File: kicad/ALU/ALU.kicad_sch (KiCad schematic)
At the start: 85 parts, among them J1 Backplane Signal, J2 Backplane Bus, J3 DIN41612_02x32_AC, J4 DIN41612_02x32_AC, U1 74LS377, U10 74LS253, U11 74LS253, U12 74LS253, U13 74LS253, U14 74LS253, U15 74LS253, U16 74LS253, U17 74F382, U18 74F382, U19 74F382, U2 74LS377, U20 74F382, U21 74F382, U22 74LS283, U23 74LS283, U24 74LS283, U25 74LS283, U26 74LS283, U27 74LS244, U28 74LS244, U29 74LS244, U3 74LS377, U30 74LS386, U31 74LS08, U32 74LS32, U33 74LS04, U34 74LS253, U35 74LS27, U36 74LS27, U37 74LS11, U38 74LS257, U39 74LS32, U4 74LS377, U5 74LS377, U6 74LS377, U7 74LS253, U8 74LS253, U9 74LS253

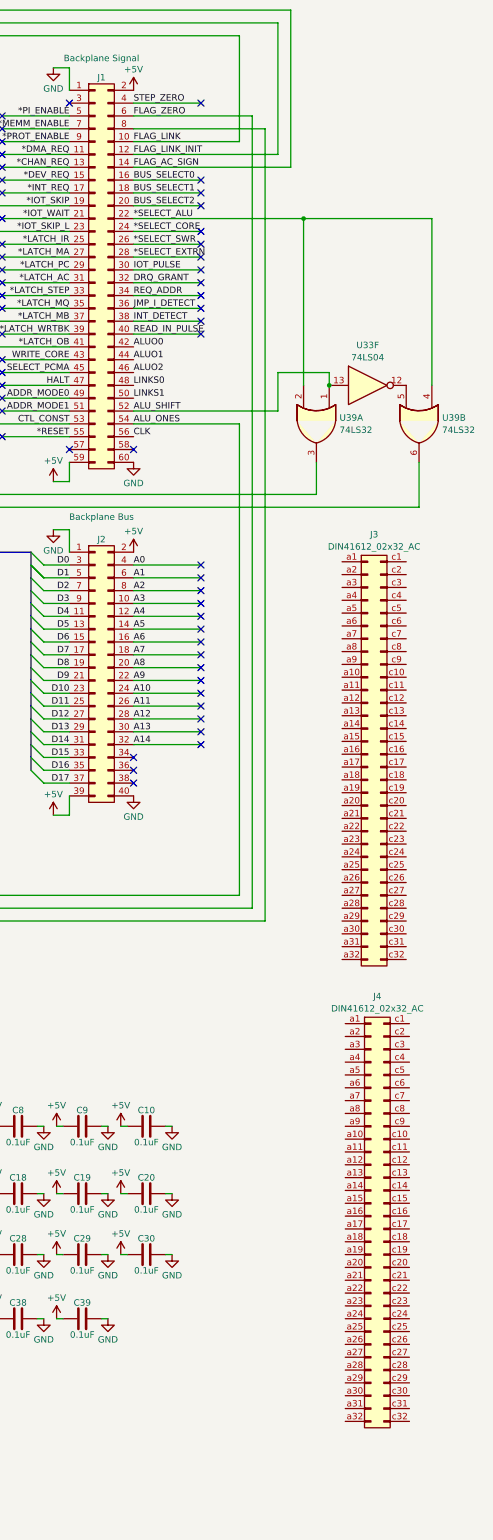
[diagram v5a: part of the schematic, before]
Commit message: Continue connector migration
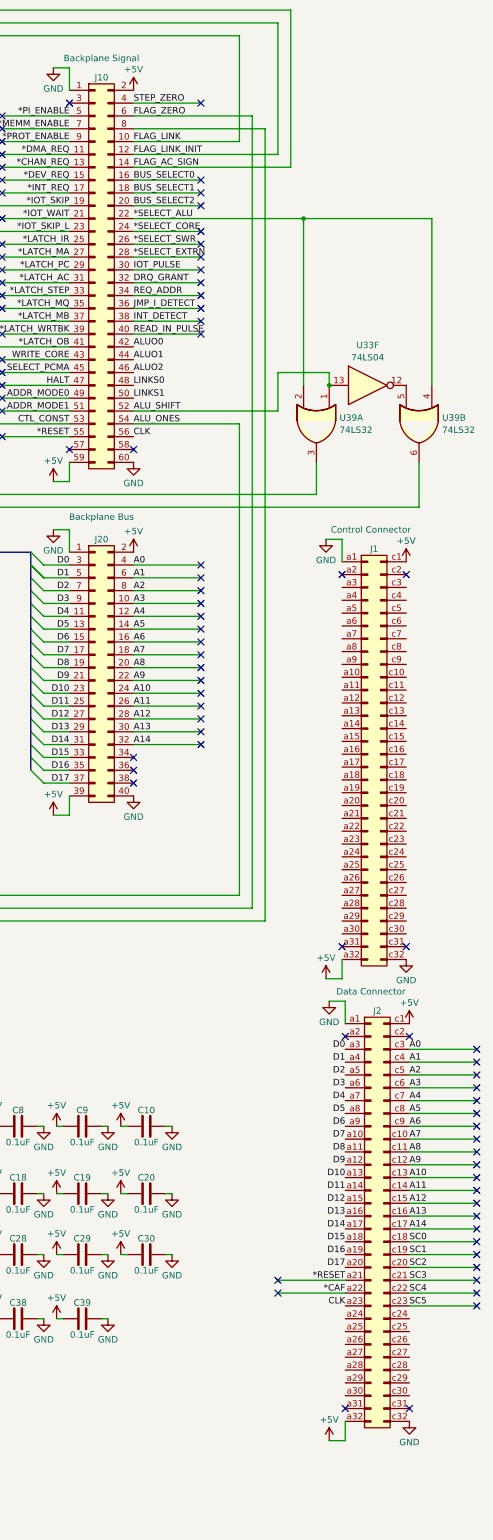
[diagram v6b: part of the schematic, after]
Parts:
- J1: renamed from J3; value DIN41612_02x32_AC -> Control Connector
- J2: renamed from J4; value DIN41612_02x32_AC -> Data Connector
- renumbered J1 to J10, J2 to J20
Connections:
- net *RESET: now also J2.a21 (Pin_a21)
- net +5V: now also J1.a32 (Pin_a32), J1.c1 (Pin_c1), J2.a32 (Pin_a32), J2.c1 (Pin_c1)
- net A0: now also J2.c3 (Pin_c3)
- net A1: now also J2.c4 (Pin_c4)
- net A10: now also J2.c13 (Pin_c13)
- net A11: now also J2.c14 (Pin_c14)
- net A12: now also J2.c15 (Pin_c15)
- net A13: now also J2.c16 (Pin_c16)
- net A14: now also J2.c17 (Pin_c17)
- net A2: now also J2.c5 (Pin_c5)
- net A3: now also J2.c6 (Pin_c6)
- net A4: now also J2.c7 (Pin_c7)
- net A5: now also J2.c8 (Pin_c8)
- net A6: now also J2.c9 (Pin_c9)
- net A7: now also J2.c10 (Pin_c10)
- net A8: now also J2.c11 (Pin_c11)
- net A9: now also J2.c12 (Pin_c12)
- net CLK: now also J2.a23 (Pin_a23)
- net D0: now also J2.a3 (Pin_a3)
- net D1: now also J2.a4 (Pin_a4)
- net D10: now also J2.a13 (Pin_a13)
- net D11: now also J2.a14 (Pin_a14)
- net D12: now also J2.a15 (Pin_a15)
- net D13: now also J2.a16 (Pin_a16)
- net D14: now also J2.a17 (Pin_a17)
- net D15: now also J2.a18 (Pin_a18)
- net D16: now also J2.a19 (Pin_a19)
- net D17: now also J2.a20 (Pin_a20)
- net D2: now also J2.a5 (Pin_a5)
- net D3: now also J2.a6 (Pin_a6)
- net D4: now also J2.a7 (Pin_a7)
- net D5: now also J2.a8 (Pin_a8)
- net D6: now also J2.a9 (Pin_a9)
- net D7: now also J2.a10 (Pin_a10)
- net D8: now also J2.a11 (Pin_a11)
- net D9: now also J2.a12 (Pin_a12)
- net GND: now also J1.a1 (Pin_a1), J1.c32 (Pin_c32), J2.a1 (Pin_a1), J2.c32 (Pin_c32)
- net *CAF: now reaches J2.a22 (Pin_a22)
- net SC0: now reaches J2.c18 (Pin_c18)
- net SC1: now reaches J2.c19 (Pin_c19)
- net SC2: now reaches J2.c20 (Pin_c20)
- net SC3: now reaches J2.c21 (Pin_c21)
- net SC4: now reaches J2.c22 (Pin_c22)
- net SC5: now reaches J2.c23 (Pin_c23)
- no-connect marks 85 -> 116

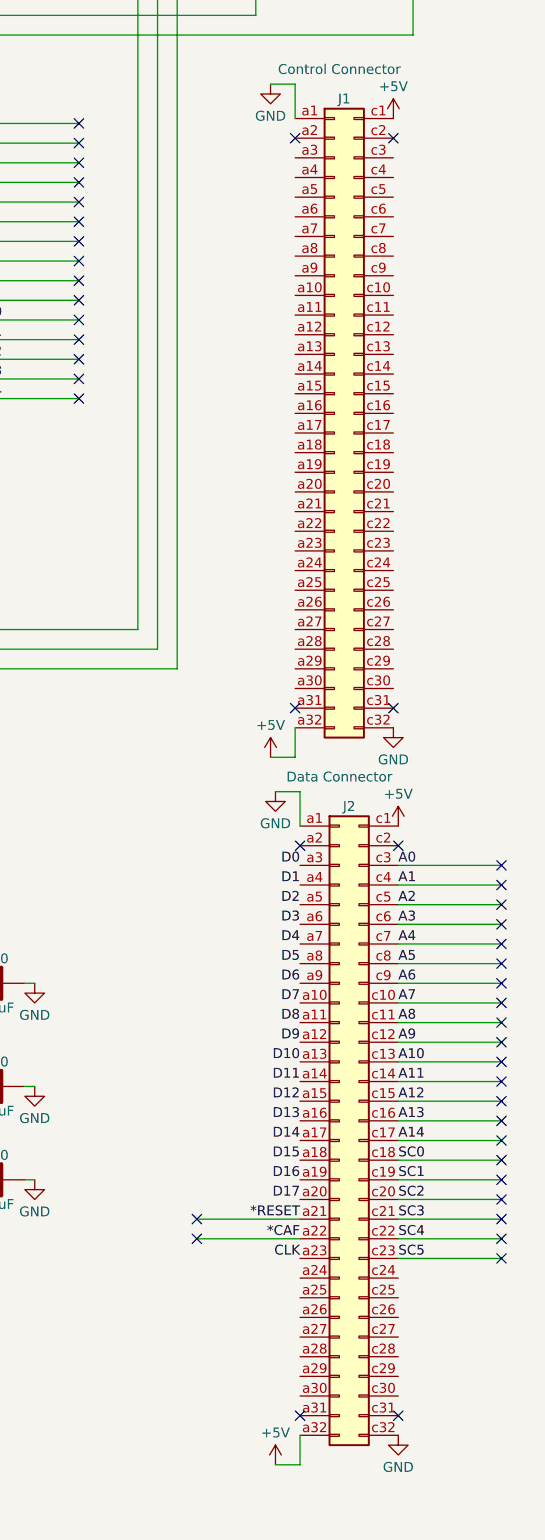
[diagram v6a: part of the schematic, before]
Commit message: Continue connector migration
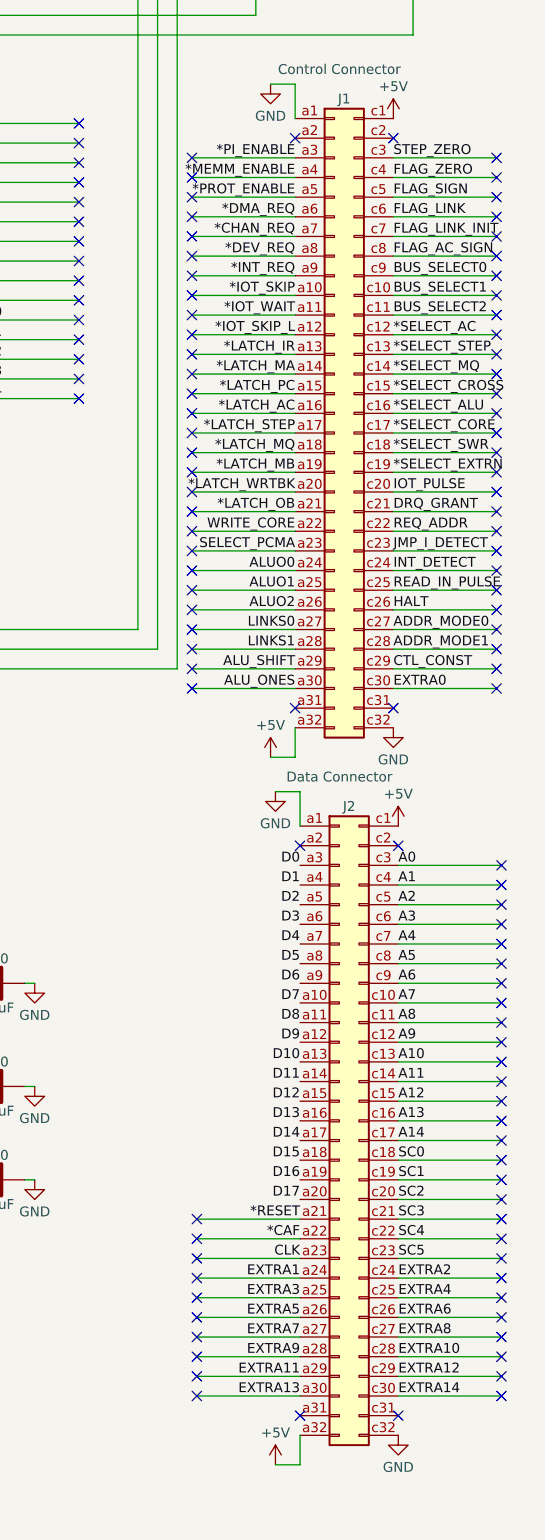
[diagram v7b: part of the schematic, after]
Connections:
- net *CHAN_REQ: now also J1.a7 (Pin_a7)
- net *DEV_REQ: now also J1.a8 (Pin_a8)
- net *DMA_REQ: now also J1.a6 (Pin_a6)
- net *INT_REQ: now also J1.a9 (Pin_a9)
- net *IOT_SKIP: now also J1.a10 (Pin_a10)
- net *IOT_SKIP_L: now also J1.a12 (Pin_a12)
- net *IOT_WAIT: now also J1.a11 (Pin_a11)
- net *LATCH_AC: now also J1.a16 (Pin_a16)
- net *LATCH_IR: now also J1.a13 (Pin_a13)
- net *LATCH_MA: now also J1.a14 (Pin_a14)
- net *LATCH_MB: now also J1.a19 (Pin_a19)
- net *LATCH_MQ: now also J1.a18 (Pin_a18)
- net *LATCH_OB: now also J1.a21 (Pin_a21)
- net *LATCH_PC: now also J1.a15 (Pin_a15)
- net *LATCH_STEP: now also J1.a17 (Pin_a17)
- net *LATCH_WRTBK: now also J1.a20 (Pin_a20)
- net *MEMM_ENABLE: now also J1.a4 (Pin_a4)
- net *PI_ENABLE: now also J1.a3 (Pin_a3)
- net *PROT_ENABLE: now also J1.a5 (Pin_a5)
- net *SELECT_ALU: now also J1.c16 (Pin_c16)
- net *SELECT_CORE: now also J1.c17 (Pin_c17)
- net *SELECT_EXTRN: now also J1.c19 (Pin_c19)
- net *SELECT_SWR: now also J1.c18 (Pin_c18)
- net ADDR_MODE0: now also J1.c27 (Pin_c27)
- net ADDR_MODE1: now also J1.c28 (Pin_c28)
- net ALUO0: now also J1.a24 (Pin_a24)
- net ALUO1: now also J1.a25 (Pin_a25)
- net ALUO2: now also J1.a26 (Pin_a26)
- net ALU_ONES: now also J1.a30 (Pin_a30)
- net ALU_SHIFT: now also J1.a29 (Pin_a29)
- net BUS_SELECT0: now also J1.c9 (Pin_c9)
- net BUS_SELECT1: now also J1.c10 (Pin_c10)
- net BUS_SELECT2: now also J1.c11 (Pin_c11)
- net CTL_CONST: now also J1.c29 (Pin_c29)
- net DRQ_GRANT: now also J1.c21 (Pin_c21)
- net FLAG_AC_SIGN: now also J1.c8 (Pin_c8)
- net FLAG_LINK: now also J1.c6 (Pin_c6)
- net FLAG_LINK_INIT: now also J1.c7 (Pin_c7)
- net FLAG_ZERO: now also J1.c4 (Pin_c4)
- net HALT: now also J1.c26 (Pin_c26)
- net INT_DETECT: now also J1.c24 (Pin_c24)
- net IOT_PULSE: now also J1.c20 (Pin_c20)
- net JMP_I_DETECT: now also J1.c23 (Pin_c23)
- net LINKS0: now also J1.a27 (Pin_a27)
- net LINKS1: now also J1.a28 (Pin_a28)
- net READ_IN_PULSE: now also J1.c25 (Pin_c25)
- net REQ_ADDR: now also J1.c22 (Pin_c22)
- net SELECT_PCMA: now also J1.a23 (Pin_a23)
- net STEP_ZERO: now also J1.c3 (Pin_c3)
- net WRITE_CORE: now also J1.a22 (Pin_a22)
- net EXTRA1: now reaches J2.a24 (Pin_a24)
- net EXTRA3: now reaches J2.a25 (Pin_a25)
- net EXTRA5: now reaches J2.a26 (Pin_a26)
- net EXTRA7: now reaches J2.a27 (Pin_a27)
- net EXTRA9: now reaches J2.a28 (Pin_a28)
- net EXTRA11: now reaches J2.a29 (Pin_a29)
- net EXTRA13: now reaches J2.a30 (Pin_a30)
- net EXTRA2: now reaches J2.c24 (Pin_c24)
- net EXTRA4: now reaches J2.c25 (Pin_c25)
- net EXTRA6: now reaches J2.c26 (Pin_c26)
- net EXTRA8: now reaches J2.c27 (Pin_c27)
- net EXTRA10: now reaches J2.c28 (Pin_c28)
- net EXTRA12: now reaches J2.c29 (Pin_c29)
- net EXTRA14: now reaches J2.c30 (Pin_c30)
- net *SELECT_AC: now reaches J1.c12 (Pin_c12)
- net *SELECT_STEP: now reaches J1.c13 (Pin_c13)
- net *SELECT_MQ: now reaches J1.c14 (Pin_c14)
- net *SELECT_CROSS: now reaches J1.c15 (Pin_c15)
- net EXTRA0: now reaches J1.c30 (Pin_c30)
- net FLAG_SIGN: now reaches J1.c5 (Pin_c5)
- no-connect marks 116 -> 187
